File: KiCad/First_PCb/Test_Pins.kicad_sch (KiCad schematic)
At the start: 9 parts

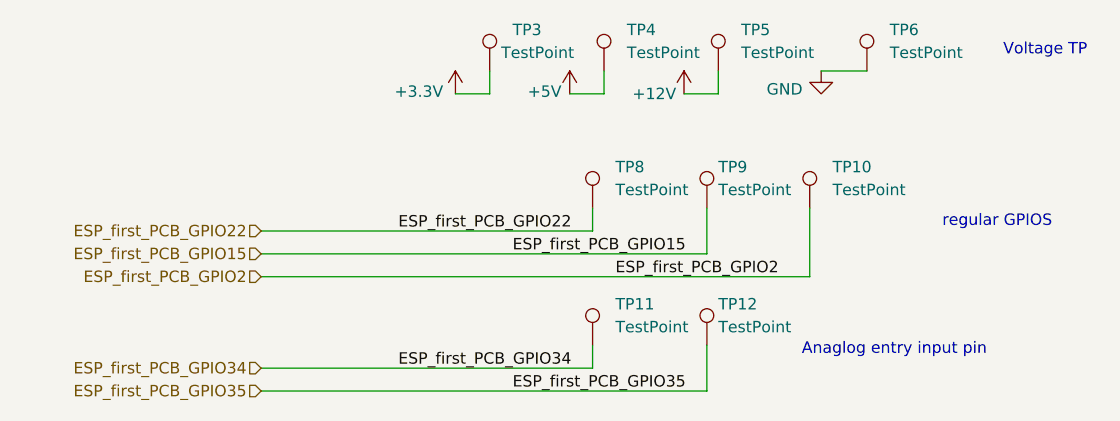
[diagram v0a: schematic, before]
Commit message: added all the kicad files & gerbers of the first pcb
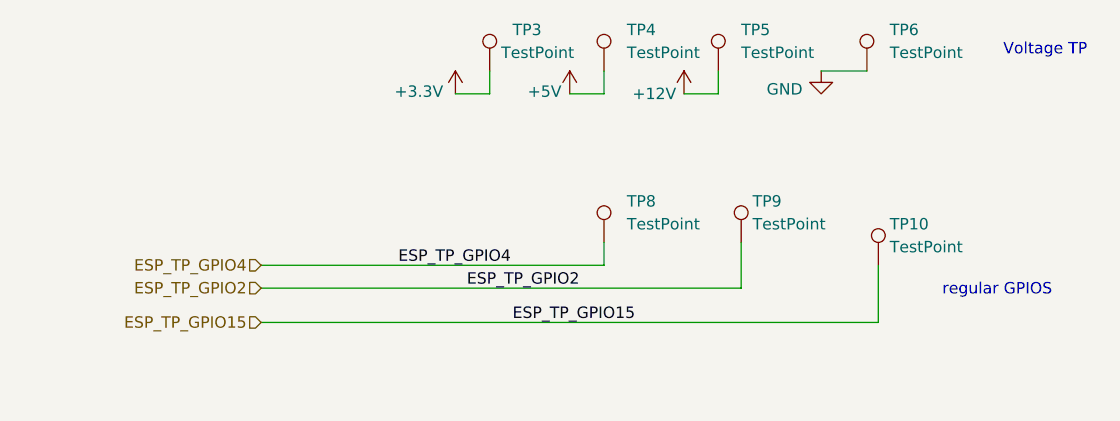
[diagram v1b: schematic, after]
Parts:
- removed TP10, TP8: TestPoint, TestPoint:TestPoint_Loop_D2.60mm_Drill1.4mm_Beaded, symbol Connector:TestPoint
- renumbered TP9 to TP10, TP11 to TP8, TP12 to TP9
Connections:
- net ESP_first_PCB_GPIO15 renamed ESP_TP_GPIO15
- net ESP_first_PCB_GPIO34 renamed ESP_TP_GPIO4
- net ESP_first_PCB_GPIO35 renamed ESP_TP_GPIO2
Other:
- note removed: "Anaglog entry input pin"
- moved on the sheet: TP10, TP8, TP9
